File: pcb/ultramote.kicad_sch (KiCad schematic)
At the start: 8 parts, among them J1 SMA-KWE902, U1 LoRa-E5

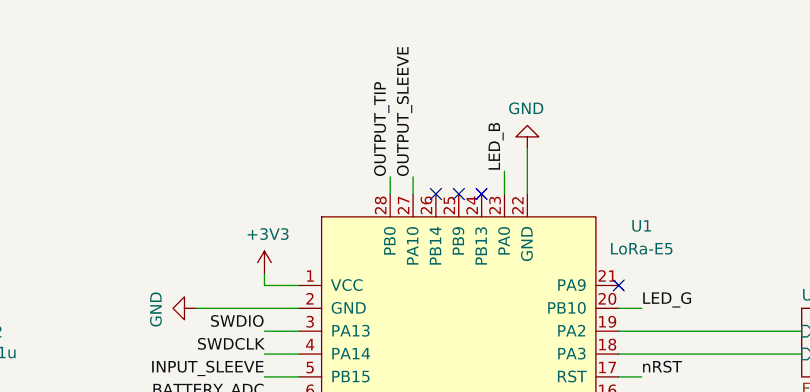
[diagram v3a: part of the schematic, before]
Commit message: Fix Pin Assignment for Output jack
closes #4
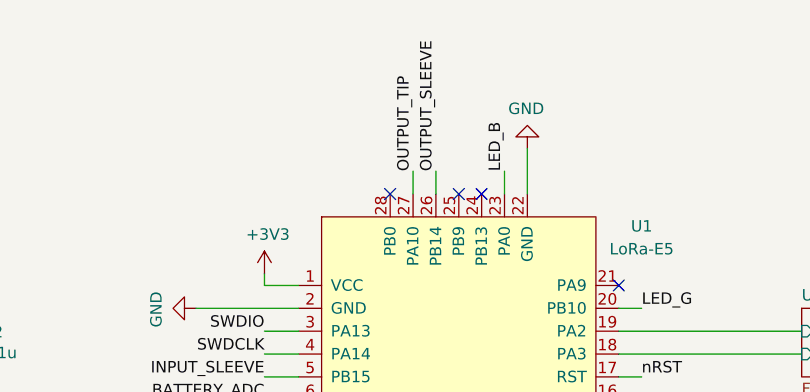
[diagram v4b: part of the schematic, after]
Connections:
- net OUTPUT_SLEEVE: now also U1.26 (PB14); no longer U1.27 (PA10)
- net OUTPUT_TIP: now also U1.27 (PA10); no longer U1.28 (PB0)
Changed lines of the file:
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@@
   )
   (no_connect (at 101.6 78.105))
+  (no_connect (at 91.44 42.545))
   (no_connect (at 99.06 42.545))
   (no_connect (at 99.06 78.105))
   (no_connect (at 96.52 78.105))
   (no_connect (at 116.84 52.705))
-  (no_connect (at 96.52 42.545))
   (no_connect (at 101.6 42.545))
   (no_connect (at 104.14 78.105))
@@
     (stroke (width 0) (type default))
   )
+  (wire (pts (xy 93.98 40.005) (xy 93.98 42.545))
+    (stroke (width 0) (type default))
+  )
   (wire (pts (xy 91.44 78.105) (xy 91.44 80.645))
     (stroke (width 0) (type default))
@@
     (stroke (width 0) (type default))
   )
+  (wire (pts (xy 96.52 40.005) (xy 96.52 42.545))
+    (stroke (width 0) (type default))
+  )
   (wire (pts (xy 43.18 52.705) (xy 43.18 55.245))
     (stroke (width 0) (type default))
   )
-  (wire (pts (xy 91.44 40.64) (xy 91.44 42.545))
-    (stroke (width 0) (type default))
-  )
   (polyline (pts (xy 75.565 133.35) (xy 75.565 196.85))
     (stroke (width 0) (type default))
@@
   )
   (wire (pts (xy 237.49 143.51) (xy 241.3 143.51))
-    (stroke (width 0) (type default))
-  )
-  (wire (pts (xy 93.98 40.64) (xy 93.98 42.545))
     (stroke (width 0) (type default))
   )
@@
     (effects (font (size 1.27 1.27)) (justify right bottom))
   )
-  (label "OUTPUT_SLEEVE" (at 93.98 40.64 90) (fields_autoplaced)
+  (label "OUTPUT_SLEEVE" (at 96.52 40.005 90) (fields_autoplaced)
     (effects (font (size 1.27 1.27)) (justify left bottom))
   )
@@
     (effects (font (size 1.27 1.27)) (justify left bottom))
   )
-  (label "OUTPUT_TIP" (at 91.44 40.64 90) (fields_autoplaced)
-    (effects (font (size 1.27 1.27)) (justify left bottom))
-  )
+  (label "OUTPUT_TIP" (at 93.98 40.005 90) (fields_autoplaced)
+    (effects (font (size 1.27 1.27)) (justify left bottom))
+  )

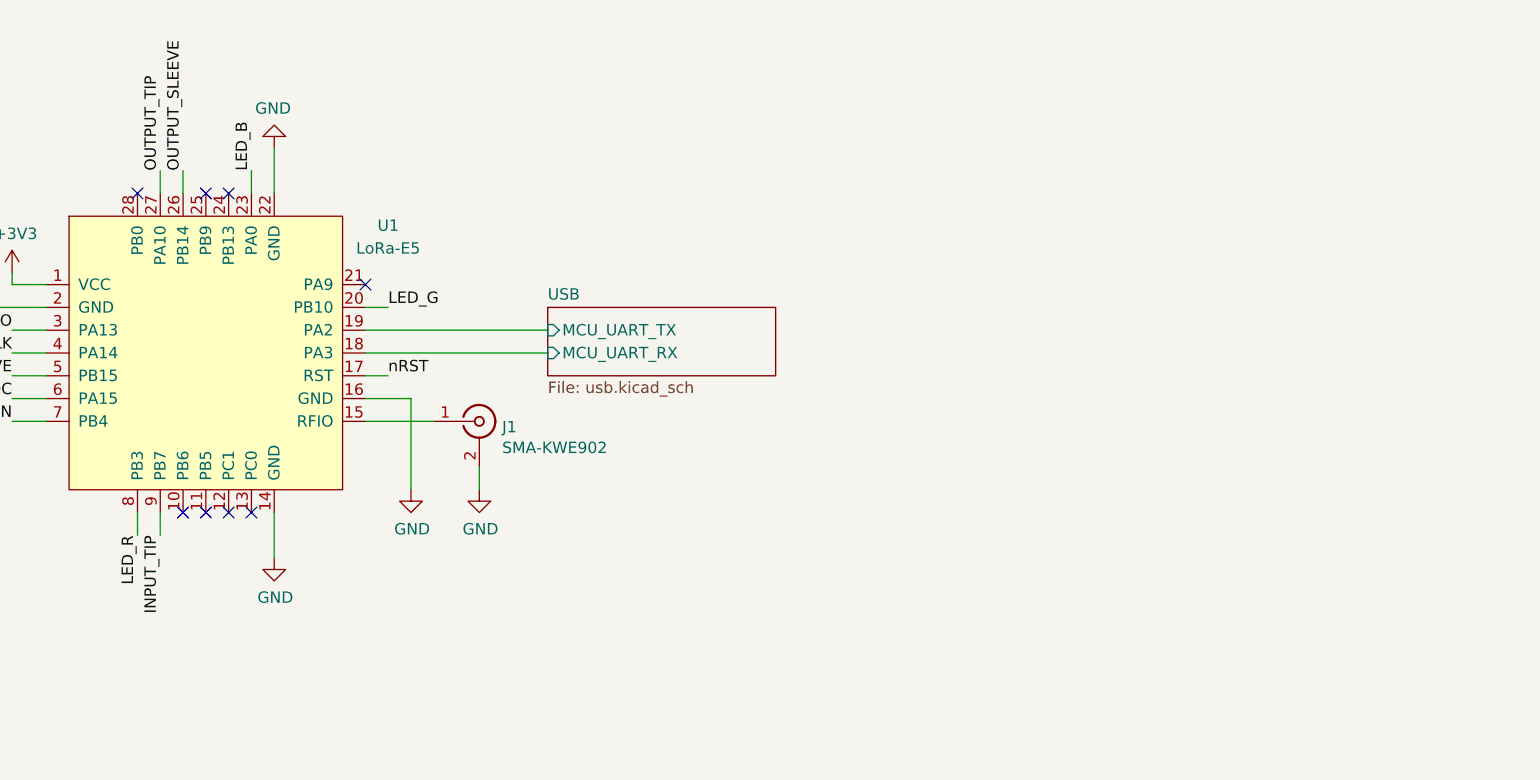
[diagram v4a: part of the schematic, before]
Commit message: Add QWIIC connector
closes #5
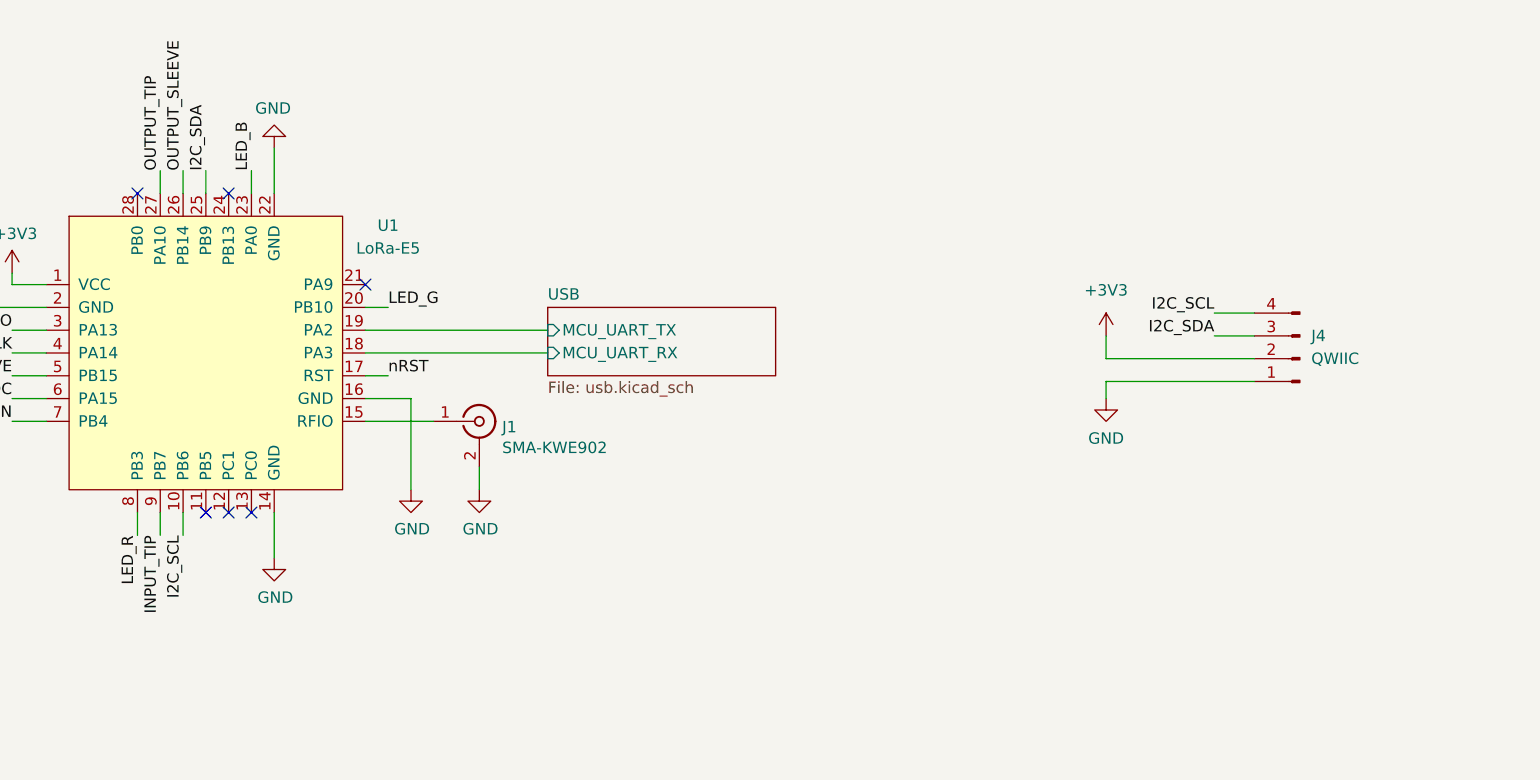
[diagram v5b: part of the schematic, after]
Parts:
- added J4: QWIIC, Connector_JST:JST_SH_BM04B-SRSS-TB_1x04-1MP_P1.00mm_Vertical, symbol Connector:Conn_01x04_Pin
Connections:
- net +3V3: now also J4.2 (Pin_2)
- net GND: now also J4.1 (Pin_1)
- net I2C_SCL: now reaches U1.10 (PB6)
- net I2C_SCL: now also J4.4 (Pin_4)
- net I2C_SDA: now reaches U1.25 (PB9)
- net I2C_SDA: now also J4.3 (Pin_3)
- no-connect marks 8 -> 6
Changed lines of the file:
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@@
   (no_connect (at 101.6 78.105))
   (no_connect (at 91.44 42.545))
-  (no_connect (at 99.06 42.545))
   (no_connect (at 99.06 78.105))
-  (no_connect (at 96.52 78.105))
   (no_connect (at 116.84 52.705))
   (no_connect (at 101.6 42.545))
@@
     (stroke (width 0) (type default))
   )
+  (wire (pts (xy 215.9 63.5) (xy 199.39 63.5))
+    (stroke (width 0) (type default))
+  )
   (wire (pts (xy 116.84 65.405) (xy 121.92 65.405))
     (stroke (width 0) (type default))
@@
     (stroke (width 0) (type default))
   )
+  (wire (pts (xy 199.39 63.5) (xy 199.39 65.405))
+    (stroke (width 0) (type default))
+  )
   (wire (pts (xy 91.44 78.105) (xy 91.44 80.645))
     (stroke (width 0) (type default))
@@
     (stroke (width 0) (type default))
   )
+  (wire (pts (xy 199.39 58.42) (xy 199.39 60.96))
+    (stroke (width 0) (type default))
+  )
   (wire (pts (xy 237.49 146.05) (xy 241.3 146.05))
     (stroke (width 0) (type default))
@@
     (stroke (width 0) (type default))
   )
+  (wire (pts (xy 199.39 60.96) (xy 215.9 60.96))
+    (stroke (width 0) (type default))
+  )
   (polyline (pts (xy 75.565 133.35) (xy 75.565 196.85))
     (stroke (width 0) (type default))
@@
     (stroke (width 0) (type default))
   )
+  (wire (pts (xy 211.455 55.88) (xy 215.9 55.88))
+    (stroke (width 0) (type default))
+  )
   (wire (pts (xy 119.38 55.245) (xy 116.84 55.245))
     (stroke (width 0) (type default))
@@
     (stroke (width 0) (type default))
   )
+  (wire (pts (xy 211.455 58.42) (xy 215.9 58.42))
+    (stroke (width 0) (type default))
+  )
   (wire (pts (xy 121.92 65.405) (xy 121.92 75.565))
     (stroke (width 0) (type default))
   )
+  (wire (pts (xy 96.52 78.105) (xy 96.52 80.645))
+    (stroke (width 0) (type default))
+  )
   (wire (pts (xy 77.47 52.705) (xy 81.28 52.705))
+    (stroke (width 0) (type default))
+  )
+  (wire (pts (xy 99.06 40.005) (xy 99.06 42.545))
     (stroke (width 0) (type default))
   )
@@
     (effects (font (size 1.27 1.27)) (justify left bottom))
   )
+  (label "I2C_SCL" (at 96.52 80.645 270) (fields_autoplaced)
+    (effects (font (size 1.27 1.27)) (justify right bottom))
+  )
   (label "LED_R" (at 241.3 140.97 0) (fields_autoplaced)
     (effects (font (size 1.27 1.27)) (justify left bottom))
@@
     (effects (font (size 1.27 1.27)) (justify left bottom))
   )
+  (label "I2C_SDA" (at 99.06 40.005 90) (fields_autoplaced)
+    (effects (font (size 1.27 1.27)) (justify left bottom))
+  )
   (label "INPUT_SLEEVE" (at 241.3 128.27 0) (fields_autoplaced)
     (effects (font (size 1.27 1.27)) (justify left bottom))
@@
     (effects (font (size 1.27 1.27)) (justify right bottom))
   )
+  (label "I2C_SDA" (at 211.455 58.42 180) (fields_autoplaced)
+    (effects (font (size 1.27 1.27)) (justify right bottom))
+  )
   (label "LED_B" (at 241.3 146.05 0) (fields_autoplaced)
     (effects (font (size 1.27 1.27)) (justify left bottom))
@@
   )
   (label "INPUT_SLEEVE" (at 77.47 62.865 180) (fields_autoplaced)
+    (effects (font (size 1.27 1.27)) (justify right bottom))
+  )
+  (label "I2C_SCL" (at 211.455 55.88 180) (fields_autoplaced)
     (effects (font (size 1.27 1.27)) (justify right bottom))
   )
@@
     )
   )
+  (symbol (lib_id "Connector:Conn_01x04_Pin") (at 220.98 60.96 180) (unit 1)
+    (in_bom yes) (on_board yes) (dnp no) (fields_autoplaced)
+    (property "Reference" "J4" (at 222.25 58.42 0)
+      (effects (font (size 1.27 1.27)) (justify right))
+    )
+    (property "Value" "QWIIC" (at 222.25 60.96 0)
+      (effects (font (size 1.27 1.27)) (justify right))
+    )
+    (property "Footprint" "Connector_JST:JST_SH_BM04B-SRSS-TB_1x04-1MP_P1.00mm_Vertical" (at 220.98 60.96 0)
+      (effects (font (size 1.27 1.27)) hide)
+    )
+    (property "Datasheet" "~" (at 220.98 60.96 0)
+      (effects (font (size 1.27 1.27)) hide)
+    )
+    (pin "1")
+    (pin "2")
+    (pin "3")
+    (pin "4")
+    (instances
+      (project "ultramote"
+        (path "/d9165d03-bf8e-4912-9bca-224da4ea4a29"
+          (reference "J4") (unit 1)
+        )
+      )
+    )
+  )
   (symbol (lib_id "Mechanical:MountingHole") (at 38.735 177.8 0) (unit 1)
     (in_bom yes) (on_board yes) (dnp no) (fields_autoplaced)
@@
         )
       )
+    )
+  )
+  (symbol (lib_name "+3V3_1") (lib_id "power:+3V3") (at 199.39 58.42 0) (unit 1)
+    (in_bom yes) (on_board yes) (dnp no) (fields_autoplaced)
+    (property "Reference" "#PWR044" (at 199.39 62.23 0)
+      (effects (font (size 1.27 1.27)) hide)
+    )
+    (property "Value" "+3V3" (at 199.39 53.34 0)
+      (effects (font (size 1.27 1.27)))
+    )
+    (property "Footprint" "" (at 199.39 58.42 0)
+      (effects (font (size 1.27 1.27)) hide)
+    )
+    (property "Datasheet" "" (at 199.39 58.42 0)
+      (effects (font (size 1.27 1.27)) hide)
+    )
+    (pin "1")
+    (instances
+      (project "ultramote"
+        (path "/d9165d03-bf8e-4912-9bca-224da4ea4a29"
+          (reference "#PWR044") (unit 1)
+        )
+      )
+    )
+  )
+  (symbol (lib_name "GND_1") (lib_id "power:GND") (at 199.39 65.405 0) (unit 1)
+    (in_bom yes) (on_board yes) (dnp no) (fields_autoplaced)
+    (property "Reference" "#PWR054" (at 199.39 71.755 0)
+      (effects (font (size 1.27 1.27)) hide)
+    )
+    (property "Value" "GND" (at 199.39 69.85 0)
+      (effects (font (size 1.27 1.27)))
+    )
+    (property "Footprint" "" (at 199.39 65.405 0)
+      (effects (font (size 1.27 1.27)) hide)
+    )
+    (property "Datasheet" "" (at 199.39 65.405 0)
+      (effects (font (size 1.27 1.27)) hide)
+    )
+    (pin "1")
+    (instances
+      (project "ultramote"
+        (path "/d9165d03-bf8e-4912-9bca-224da4ea4a29"
+          (reference "#PWR054") (unit 1)
+        )
+      )
